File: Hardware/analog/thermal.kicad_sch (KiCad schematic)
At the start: 13 parts

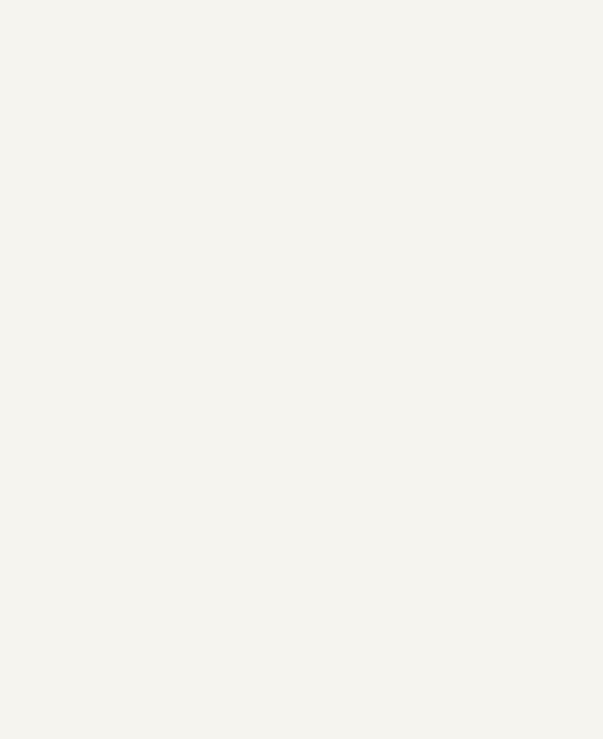
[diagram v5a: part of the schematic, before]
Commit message: Temperature sensing & cleanup for analog board
- Added the auxiliary temperature sensing ADC, and routed it to the
  analog temperature sensors on the front and rear of the MOSFET
  heatsink

- Added an LM75 sensor to measure the analog board ambient temperature
  (for better temperature control/fan control)

  This may end up being a DNP item if it's not really useful or
  otherwise necessary.

- Fixes to a few symbols (namely pin directions) to pass ERC
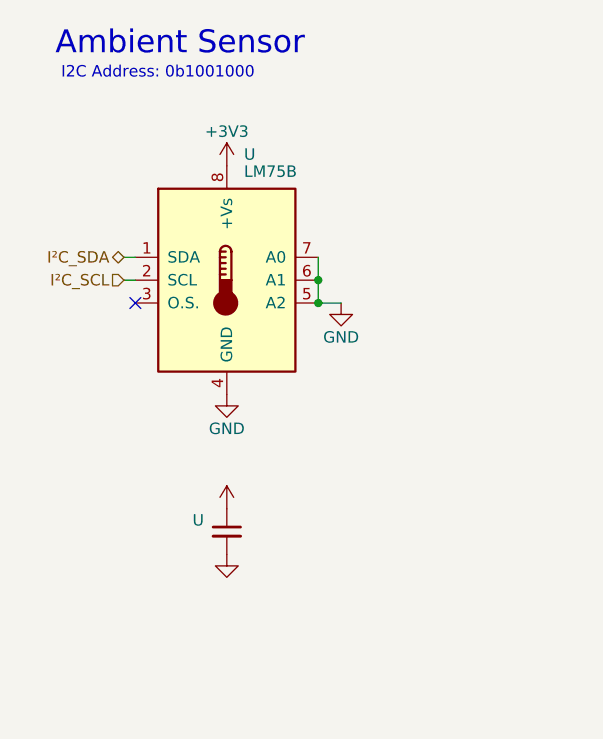
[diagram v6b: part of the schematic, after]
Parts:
- added U: (no value), symbol Device:C_Small
- added U: LM75B, symbol Sensor_Temperature:LM75B
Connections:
- new net +3V3: U.1, U.8 (+Vs)
- new net GND: U.2, U.4 (GND), U.5 (A2), U.6 (A1), U.7 (A0)
- new net I²C_SCL: U.2 (SCL)
- new net I²C_SDA: U.1 (SDA)
- no-connect marks 0 -> 1
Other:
- note added: "Ambient Sensor"
- note added: "I2C Address: 0b1001000"
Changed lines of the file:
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@@
     (rev "1")
   )
+  (junction (at 54.61 43.815) (diameter 0) (color 0 0 0 0)
+  )
   (junction (at 214.63 102.87) (diameter 0) (color 0 0 0 0)
   )
@@
   (junction (at 236.22 88.9) (diameter 0) (color 0 0 0 0)
   )
+  (junction (at 54.61 46.355) (diameter 0) (color 0 0 0 0)
+  )
   (junction (at 209.55 88.9) (diameter 0) (color 0 0 0 0)
   )
+  (no_connect (at 34.29 46.355))
   (wire (pts (xy 191.77 45.72) (xy 198.12 45.72))
     (stroke (width 0) (type default))
   )
+  (wire (pts (xy 33.02 41.275) (xy 34.29 41.275))
+    (stroke (width 0) (type default))
+  )
   (wire (pts (xy 214.63 102.87) (xy 228.6 102.87))
     (stroke (width 0) (type default))
@@
     (stroke (width 0) (type default))
   )
+  (wire (pts (xy 33.02 43.815) (xy 34.29 43.815))
+    (stroke (width 0) (type default))
+  )
   (wire (pts (xy 252.73 101.6) (xy 252.73 105.41))
     (stroke (width 0) (type default))
   )
+  (wire (pts (xy 54.61 46.355) (xy 57.15 46.355))
+    (stroke (width 0) (type default))
+  )
   (wire (pts (xy 219.71 97.79) (xy 228.6 97.79))
     (stroke (width 0) (type default))
@@
     (stroke (width 0) (type default))
   )
+  (wire (pts (xy 54.61 41.275) (xy 54.61 43.815))
+    (stroke (width 0) (type default))
+  )
   (wire (pts (xy 207.01 107.95) (xy 197.485 107.95))
     (stroke (width 0) (type default))
@@
   )
   (wire (pts (xy 209.55 60.325) (xy 219.075 60.325))
+    (stroke (width 0) (type default))
+  )
+  (wire (pts (xy 54.61 43.815) (xy 54.61 46.355))
     (stroke (width 0) (type default))
   )
@@
     (effects (font (size 2.54 2.54)) (justify left bottom))
   )
+  (text "Ambient Sensor" (at 25.4 19.05 0)
+    (effects (font (size 2.54 2.54)) (justify left bottom))
+  )
   (text "Host loads regs, fan at 100% duty\n(Because Q501 inverts, this means 0% fan speed)\nNOTE: Host needs to configure invert bit"
     (at 195.58 68.58 0)
+    (effects (font (size 1.27 1.27)) (justify left bottom))
+  )
+  (text "I2C Address: 0b1001000" (at 26.035 21.59 0)
     (effects (font (size 1.27 1.27)) (justify left bottom))
   )
@@
       (effects (font (size 1.27 1.27)) (justify right) hide)
     )
+  )
+  (hierarchical_label "I²C_SDA" (shape bidirectional) (at 33.02 41.275 180) (fields_autoplaced)
+    (effects (font (size 1.27 1.27)) (justify right))
+  )
+  (hierarchical_label "I²C_SCL" (shape input) (at 33.02 43.815 180) (fields_autoplaced)
+    (effects (font (size 1.27 1.27)) (justify right))
+  )
+  (symbol (lib_id "power:+3V3") (at 44.45 69.215 0) (unit 1)
+    (in_bom yes) (on_board yes)
+    (default_instance (reference "U") (unit 1) (value "") (footprint ""))
+    (property "Reference" "U" (id 0) (at 44.45 73.025 0)
+      (effects (font (size 1.27 1.27)) hide)
+    )
+    (property "Value" "" (id 1) (at 44.45 64.77 0)
+      (effects (font (size 1.27 1.27)))
+    )
+    (property "Footprint" "" (id 2) (at 44.45 69.215 0)
+      (effects (font (size 1.27 1.27)) hide)
+    )
+    (property "Datasheet" "" (id 3) (at 44.45 69.215 0)
+      (effects (font (size 1.27 1.27)) hide)
+    )
+    (pin "1")
   )
   (symbol (lib_id "power:+3.3VP") (at 204.47 60.325 90) (unit 1)
@@
     (pin "2")
   )
+  (symbol (lib_id "Device:C_Small") (at 44.45 71.755 0) (unit 1)
+    (in_bom yes) (on_board yes) (fields_autoplaced)
+    (default_instance (reference "U") (unit 1) (value "") (footprint ""))
+    (property "Reference" "U" (id 0) (at 41.91 70.4912 0)
+      (effects (font (size 1.27 1.27)) (justify right))
+    )
+    (property "Value" "" (id 1) (at 41.91 73.0312 0)
+      (effects (font (size 1.27 1.27)) (justify right))
+    )
+    (property "Footprint" "" (id 2) (at 44.45 71.755 0)
+      (effects (font (size 1.27 1.27)) hide)
+    )
+    (property "Datasheet" "~" (id 3) (at 44.45 71.755 0)
+      (effects (font (size 1.27 1.27)) hide)
+    )
+    (pin "1")
+    (pin "2")
+  )
   (symbol (lib_id "Connector_Generic:Conn_01x01") (at 244.475 27.94 0) (mirror y) (unit 1)
     (in_bom yes) (on_board yes)
@@
     (pin "1")
   )
+  (symbol (lib_id "power:GND") (at 44.45 74.295 0) (unit 1)
+    (in_bom yes) (on_board yes)
+    (default_instance (reference "U") (unit 1) (value "") (footprint ""))
+    (property "Reference" "U" (id 0) (at 44.45 80.645 0)
+      (effects (font (size 1.27 1.27)) hide)
+    )
+    (property "Value" "" (id 1) (at 44.45 78.74 0)
+      (effects (font (size 1.27 1.27)))
+    )
+    (property "Footprint" "" (id 2) (at 44.45 74.295 0)
+      (effects (font (size 1.27 1.27)) hide)
+    )
+    (property "Datasheet" "" (id 3) (at 44.45 74.295 0)
+      (effects (font (size 1.27 1.27)) hide)
+    )
+    (pin "1")
+  )
   (symbol (lib_id "Device:R_Small") (at 207.01 60.325 90) (unit 1)
     (in_bom yes) (on_board yes) (fields_autoplaced)
@@
     (pin "2")
   )
+  (symbol (lib_id "power:GND") (at 44.45 56.515 0) (unit 1)
+    (in_bom yes) (on_board yes)
+    (default_instance (reference "#PWR") (unit 1) (value "GND") (footprint ""))
+    (property "Reference" "#PWR" (id 0) (at 44.45 62.865 0)
+      (effects (font (size 1.27 1.27)) hide)
+    )
+    (property "Value" "GND" (id 1) (at 44.45 60.325 0)
+      (effects (font (size 1.27 1.27)))
+    )
+    (property "Footprint" "" (id 2) (at 44.45 56.515 0)
+      (effects (font (size 1.27 1.27)) hide)
+    )
+    (property "Datasheet" "" (id 3) (at 44.45 56.515 0)
+      (effects (font (size 1.27 1.27)) hide)
+    )
+    (pin "1")
+  )
+  (symbol (lib_id "Sensor_Temperature:LM75B") (at 44.45 43.815 0) (unit 1)
+    (in_bom yes) (on_board yes)
+    (default_instance (reference "U") (unit 1) (value "LM75B") (footprint ""))
+    (property "Reference" "U" (id 0) (at 46.355 29.845 0)
+      (effects (font (size 1.27 1.27)) (justify left))
+    )
+    (property "Value" "LM75B" (id 1) (at 46.355 31.75 0)
+      (effects (font (size 1.27 1.27)) (justify left))
+    )
+    (property "Footprint" "" (id 2) (at 44.45 43.815 0)
+      (effects (font (size 1.27 1.27)) hide)
+    )
+    (property "Datasheet" "http://www.ti.com/lit/ds/symlink/lm75b.pdf" (id 3) (at 44.45 43.815 0)
+      (effects (font (size 1.27 1.27)) hide)
+    )
+    (property "MPN" "AT30TS74-SS8M-B" (id 4) (at 44.45 43.815 0)
+      (effects (font (size 1.27 1.27)) hide)
+    )
+    (pin "1")
+    (pin "2")
+    (pin "3")
+    (pin "4")
+    (pin "5")
+    (pin "6")
+    (pin "7")
+    (pin "8")
+  )
   (symbol (lib_id "power:+3.3VP") (at 191.77 45.72 90) (unit 1)
     (in_bom yes) (on_board yes)
@@
     (pin "1")
     (pin "2")
+  )
+  (symbol (lib_id "power:+3V3") (at 44.45 31.115 0) (unit 1)
+    (in_bom yes) (on_board yes)
+    (default_instance (reference "#PWR") (unit 1) (value "+3V3") (footprint ""))
+    (property "Reference" "#PWR" (id 0) (at 44.45 34.925 0)
+      (effects (font (size 1.27 1.27)) hide)
+    )
+    (property "Value" "+3V3" (id 1) (at 44.45 27.305 0)
+      (effects (font (size 1.27 1.27)))
+    )
+    (property "Footprint" "" (id 2) (at 44.45 31.115 0)
+      (effects (font (size 1.27 1.27)) hide)
+    )
+    (property "Datasheet" "" (id 3) (at 44.45 31.115 0)
+      (effects (font (size 1.27 1.27)) hide)
+    )
+    (pin "1")
   )
   (symbol (lib_id "Transistor_BJT:MMBT3904") (at 212.09 107.95 0) (unit 1)
@@
     (pin "2")
   )
+  (symbol (lib_id "power:GND") (at 57.15 46.355 0) (unit 1)
+    (in_bom yes) (on_board yes)
+    (default_instance (reference "#PWR") (unit 1) (value "GND") (footprint ""))
+    (property "Reference" "#PWR" (id 0) (at 57.15 52.705 0)
+      (effects (font (size 1.27 1.27)) hide)
+    )
+    (property "Value" "GND" (id 1) (at 57.15 50.165 0)
+      (effects (font (size 1.27 1.27)))
+    )
+    (property "Footprint" "" (id 2) (at 57.15 46.355 0)
+      (effects (font (size 1.27 1.27)) hide)
+    )
+    (property "Datasheet" "" (id 3) (at 57.15 46.355 0)
+      (effects (font (size 1.27 1.27)) hide)
+    )
+    (pin "1")
+  )
   (symbol (lib_id "power:GND2") (at 209.55 93.98 0) (unit 1)
